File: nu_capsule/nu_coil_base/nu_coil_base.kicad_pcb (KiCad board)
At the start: 2 copper layers, 7.9 x 9 mm, 6 parts

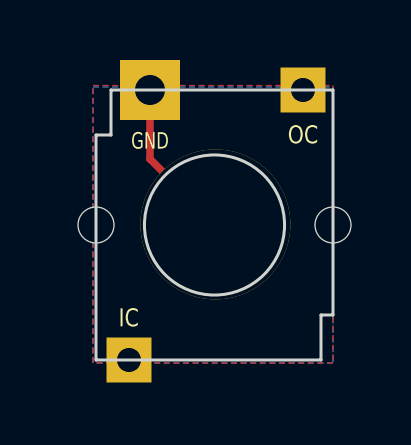
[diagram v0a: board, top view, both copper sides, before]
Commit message: Coil base panel
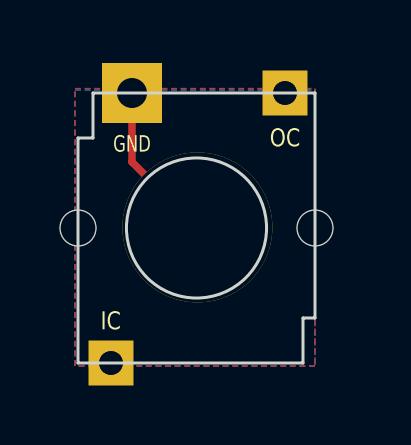
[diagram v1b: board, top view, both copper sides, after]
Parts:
- moved Magnet_PAD1 0.61 mm to (137.5, 92.5)
- moved FPAD1 0.61 mm to (140.4, 88.0)
- moved Gnd-Pad1 0.61 mm to (135.3, 88.0)
- moved REF** 0.61 mm to (133.5, 92.5)
- moved REF** 0.61 mm to (141.4, 92.5)
- moved SPAD1 0.61 mm to (134.6, 97.0)
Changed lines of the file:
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@@
   )
   (module cycfi_library:hole_1.2mm (layer F.Cu)
-    (at 134.1 92.4)
+    (at 133.5 92.5)
     (descr "Mounting Hole 2.1mm, no annular")
     (tags "mounting hole 2.1mm no annular")
@@
       (effects (font (size 1 1) (thickness 0.15)))
     )
+    (fp_circle (center 0 0) (end 0.6 0) (layer F.CrtYd) (width 0.05))
     (fp_text user %R (at 0.3 0) (layer F.Fab) hide
       (effects (font (size 1 1) (thickness 0.15)))
     )
-    (fp_circle (center 0 0) (end 0.6 0) (layer F.CrtYd) (width 0.05))
     (pad "" np_thru_hole circle (at 0 0) (size 1.2 1.2) (drill 1.2) (layers *.Cu *.Mask))
   )
   (module cycfi_library:hole_1.2mm (layer F.Cu)
-    (at 142 92.4)
+    (at 141.4 92.5)
     (descr "Mounting Hole 2.1mm, no annular")
     (tags "mounting hole 2.1mm no annular")
@@
   )
   (module cycfi_library:single-pad-1.5x1.5-th (layer F.Cu)
-    (at 135.2 96.9)
+    (at 134.6 97)
     (fp_text reference SPAD1 (at 0 2.54) (layer F.SilkS) hide
       (effects (font (size 1 1) (thickness 0.15)))
@@
   )
   (module cycfi_library:nu_magnet_pad (layer F.Cu)
-    (at 138.08 92.38)
+    (at 137.48 92.48)
     (fp_text reference Magnet_PAD1 (at 0 4) (layer F.SilkS) hide
       (effects (font (size 1 1) (thickness 0.15)))
@@
   )
   (module cycfi_library:single-pad-2x2-th (layer F.Cu)
-    (at 135.9 87.9)
+    (at 135.3 88)
     (fp_text reference Gnd-Pad1 (at 0 2.54) (layer F.SilkS) hide
       (effects (font (size 1 1) (thickness 0.15)))
@@
   )
   (module cycfi_library:single-pad-1.5x1.5-th (layer F.Cu)
-    (at 141 87.9 90)
+    (at 140.4 88 90)
     (fp_text reference FPAD1 (at 0 2.54 90) (layer F.SilkS) hide
       (effects (font (size 1 1) (thickness 0.15)))
@@
       (net 2 OC))
   )
-  (gr_line (start 134.6 87.9) (end 142 87.9) (angle 90) (layer Edge.Cuts) (width 0.1))
-  (gr_line (start 141.6 95.4) (end 142 95.4) (angle 90) (layer Edge.Cuts) (width 0.1))
-  (gr_circle (center 138.05 92.4) (end 140.385 92.4) (layer Edge.Cuts) (width 0.1))
-  (gr_line (start 142 95.4) (end 142 87.9) (layer Edge.Cuts) (width 0.1))
-  (gr_line (start 134.6 87.9) (end 134.6 89.4) (layer Edge.Cuts) (width 0.1))
-  (gr_line (start 134.6 89.4) (end 134.1 89.4) (layer Edge.Cuts) (width 0.1))
-  (gr_line (start 134.1 89.4) (end 134.1 96.9) (layer Edge.Cuts) (width 0.1))
-  (gr_circle (center 138.06 92.4) (end 140.56 92.4) (layer Dwgs.User) (width 0.1))
-  (gr_text GND (at 135.9 89.6) (layer F.SilkS)
+  (gr_line (start 134 88) (end 141.4 88) (angle 90) (layer Edge.Cuts) (width 0.1))
+  (gr_line (start 141 95.5) (end 141.4 95.5) (angle 90) (layer Edge.Cuts) (width 0.1))
+  (gr_circle (center 137.45 92.5) (end 139.785 92.5) (layer Edge.Cuts) (width 0.1))
+  (gr_line (start 141.4 95.5) (end 141.4 88) (layer Edge.Cuts) (width 0.1))
+  (gr_line (start 134 88) (end 134 89.5) (layer Edge.Cuts) (width 0.1))
+  (gr_line (start 134 89.5) (end 133.5 89.5) (layer Edge.Cuts) (width 0.1))
+  (gr_line (start 133.5 89.5) (end 133.5 97) (layer Edge.Cuts) (width 0.1))
+  (gr_circle (center 137.45 92.5) (end 139.95 92.5) (layer Dwgs.User) (width 0.1))
+  (gr_text GND (at 135.3 89.7) (layer F.SilkS)
     (effects (font (size 0.55 0.4) (thickness 0.07)))
   )
-  (gr_text IC (at 135.19 95.5) (layer F.SilkS)
+  (gr_text IC (at 134.59 95.6) (layer F.SilkS)
     (effects (font (size 0.6 0.5) (thickness 0.07)))
   )
-  (gr_text OC (at 141 89.4) (layer F.SilkS)
+  (gr_text OC (at 140.4 89.5) (layer F.SilkS)
     (effects (font (size 0.6 0.5) (thickness 0.07)))
   )
-  (gr_circle (center 138.04 92.3) (end 138.04 88.3) (layer Dwgs.User) (width 0.05))
-  (gr_line (start 141.6 96.9) (end 134.1 96.9) (angle 90) (layer Edge.Cuts) (width 0.1))
-  (gr_line (start 137.99 87.9) (end 137.99 96.9) (angle 90) (layer Dwgs.User) (width 0.05))
-  (gr_line (start 134.09 92.4) (end 142.04 92.4) (angle 90) (layer Dwgs.User) (width 0.05))
-  (gr_line (start 141.6 95.4) (end 141.6 96.9) (angle 90) (layer Edge.Cuts) (width 0.1))
-  (segment (start 135.9 90.2) (end 138.08 92.38) (width 0.25) (layer F.Cu) (net 1))
-  (segment (start 135.9 87.9) (end 135.9 90.2) (width 0.25) (layer F.Cu) (net 1))
+  (gr_circle (center 137.45 92.5) (end 141.45 92.5) (layer Dwgs.User) (width 0.1))
+  (gr_line (start 141 97) (end 133.5 97) (angle 90) (layer Edge.Cuts) (width 0.1))
+  (gr_line (start 137.45 88) (end 137.45 97) (angle 90) (layer Dwgs.User) (width 0.1))
+  (gr_line (start 133.49 92.5) (end 141.44 92.5) (angle 90) (layer Dwgs.User) (width 0.1))
+  (gr_line (start 141 95.5) (end 141 97) (angle 90) (layer Edge.Cuts) (width 0.1))
+  (segment (start 135.3 90.3) (end 137.48 92.48) (width 0.25) (layer F.Cu) (net 1))
+  (segment (start 135.3 88) (end 135.3 90.3) (width 0.25) (layer F.Cu) (net 1))
   (zone (net 1) (net_name GND) (layer F.Cu) (hatch edge 0.508)
     (connect_pads yes (clearance 0.15))
@@
     (polygon
       (pts
-        (xy 142 97) (xy 134 97) (xy 134 87.75) (xy 142 87.75)
+        (xy 141.4 97.1) (xy 133.4 97.1) (xy 133.4 87.85) (xy 141.4 87.85)
       )
     )
@@
     (polygon
       (pts
-        (xy 142 97) (xy 134 97) (xy 134 87.8) (xy 142 87.8)
+        (xy 141.4 97.1) (xy 133.4 97.1) (xy 133.4 87.9) (xy 141.4 87.9)
       )
     )

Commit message: updated; removed side slots
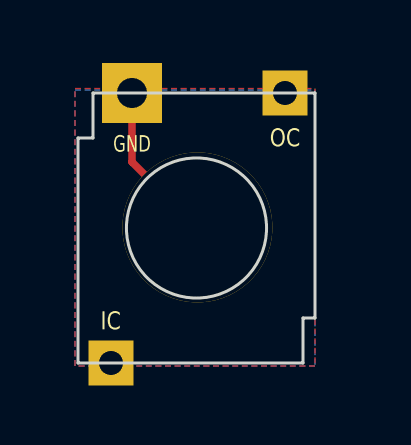
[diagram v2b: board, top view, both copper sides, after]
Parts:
- removed REF** (x2): hole_1.2mm, cycfi_library:hole_1.2mm
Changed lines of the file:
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@@
     (tracks 2)
     (zones 0)
-    (modules 6)
+    (modules 4)
     (nets 4)
   )
@@
     (add_net OC)
   )
-  (module cycfi_library:hole_1.2mm (layer F.Cu)
-    (at 133.5 92.5)
-    (descr "Mounting Hole 2.1mm, no annular")
-    (tags "mounting hole 2.1mm no annular")
-    (attr virtual)
-    (fp_text reference REF** (at 0 -3.2) (layer F.SilkS) hide
-      (effects (font (size 1 1) (thickness 0.15)))
-    )
-    (fp_text value hole_1.2mm (at 0 3.2) (layer F.Fab)
-      (effects (font (size 1 1) (thickness 0.15)))
-    )
-    (fp_circle (center 0 0) (end 0.6 0) (layer F.CrtYd) (width 0.05))
-    (fp_text user %R (at 0.3 0) (layer F.Fab) hide
-      (effects (font (size 1 1) (thickness 0.15)))
-    )
-    (pad "" np_thru_hole circle (at 0 0) (size 1.2 1.2) (drill 1.2) (layers *.Cu *.Mask))
-  )
-  (module cycfi_library:hole_1.2mm (layer F.Cu)
-    (at 141.4 92.5)
-    (descr "Mounting Hole 2.1mm, no annular")
-    (tags "mounting hole 2.1mm no annular")
-    (attr virtual)
-    (fp_text reference REF** (at 0 -3.2) (layer F.SilkS) hide
-      (effects (font (size 1 1) (thickness 0.15)))
-    )
-    (fp_text value hole_1.2mm (at 0 3.2) (layer F.Fab)
-      (effects (font (size 1 1) (thickness 0.15)))
-    )
-    (fp_circle (center 0 0) (end 0.6 0) (layer F.CrtYd) (width 0.05))
-    (fp_text user %R (at 0.3 0) (layer F.Fab) hide
-      (effects (font (size 1 1) (thickness 0.15)))
-    )
-    (pad "" np_thru_hole circle (at 0 0) (size 1.2 1.2) (drill 1.2) (layers *.Cu *.Mask))
-  )
   (module cycfi_library:single-pad-1.5x1.5-th (layer F.Cu)

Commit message: moved v-cut in the edge layer
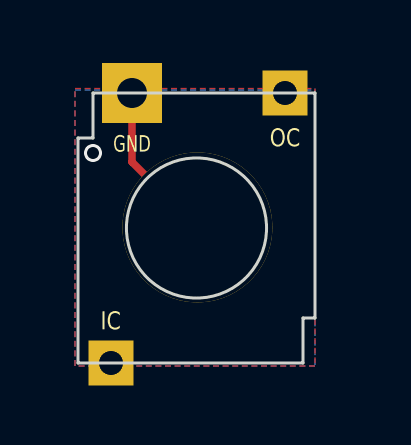
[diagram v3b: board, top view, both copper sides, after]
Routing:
- net GND: vias 0 -> 1
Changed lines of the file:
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@@
     (thickness 1.6)
     (drawings 16)
-    (tracks 2)
+    (tracks 3)
     (zones 0)
     (modules 4)
@@
   (page A4)
   (layers
-    (0 F.Cu signal)
+    (0 F.Cu signal hide)
     (31 B.Cu signal)
     (32 B.Adhes user)
@@
   (segment (start 135.3 90.3) (end 137.48 92.48) (width 0.25) (layer F.Cu) (net 1))
   (segment (start 135.3 88) (end 135.3 90.3) (width 0.25) (layer F.Cu) (net 1))
+  (via (at 134 90) (size 0.6) (drill 0.4) (layers F.Cu B.Cu) (net 1))
   (zone (net 1) (net_name GND) (layer F.Cu) (hatch edge 0.508)
     (connect_pads yes (clearance 0.15))
